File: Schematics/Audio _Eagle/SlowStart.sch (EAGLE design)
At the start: 19 parts

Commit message: slow start updates
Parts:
- added U$4: FUSE, Amplifier_Parts:FUSE
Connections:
- new net N$6: U$2.S2
- net N$1: no longer U$2.S2
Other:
- note added: "fuse will go here"
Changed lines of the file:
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@@
 <part name="GND1" library="supply1" deviceset="GND" device=""/>
 <part name="R2" library="resistor" deviceset="R-US_" device="0207/15" value="100"/>
+<part name="U$4" library="Amplifier_Parts" deviceset="FUSE" device=""/>
 </parts>
 <sheets>
@@
 <text x="81.28" y="71.12" size="1.778" layer="97">Vac+</text>
 <text x="58.42" y="43.18" size="1.778" layer="97">Vac-</text>
+<text x="-10.16" y="73.66" size="1.778" layer="97">fuse will go here</text>
 </plain>
 <instances>
@@
 <instance part="GND1" gate="1" x="81.28" y="50.8" rot="R270"/>
 <instance part="R2" gate="G$1" x="88.9" y="50.8"/>
+<instance part="U$4" gate="G$1" x="5.08" y="66.04"/>
 </instances>
 <busses>
@@
 <net name="N$1" class="0">
 <segment>
-<pinref part="U$2" gate="G$1" pin="S2"/>
-<wire x1="-17.78" y1="71.12" x2="-12.7" y2="71.12" width="0.1524" layer="91"/>
-<wire x1="-12.7" y1="71.12" x2="-12.7" y2="76.2" width="0.1524" layer="91"/>
 <pinref part="U$2" gate="G$1" pin="S3"/>
-<wire x1="-12.7" y1="76.2" x2="-17.78" y2="76.2" width="0.1524" layer="91"/>
+<wire x1="12.7" y1="66.04" x2="12.7" y2="76.2" width="0.1524" layer="91"/>
+<wire x1="12.7" y1="76.2" x2="-17.78" y2="76.2" width="0.1524" layer="91"/>
 </segment>
 </net>
@@
 </segment>
 </net>
+<net name="N$6" class="0">
+<segment>
+<pinref part="U$2" gate="G$1" pin="S2"/>
+<wire x1="-17.78" y1="71.12" x2="-2.54" y2="71.12" width="0.1524" layer="91"/>
+<wire x1="-2.54" y1="71.12" x2="-2.54" y2="66.04" width="0.1524" layer="91"/>
+</segment>
+</net>

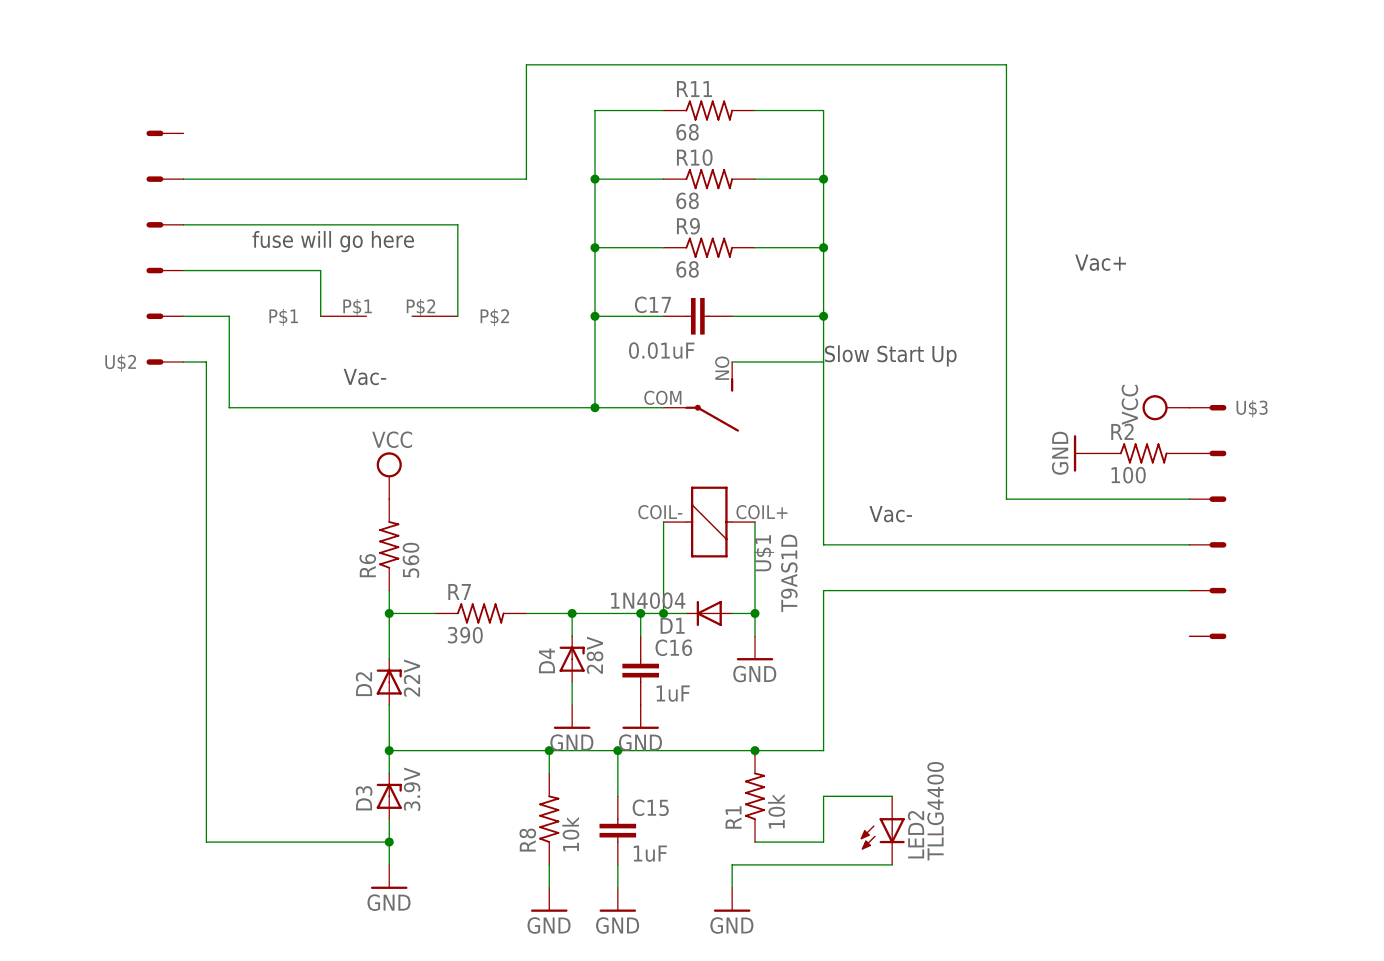
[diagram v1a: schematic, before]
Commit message: updated block diagram
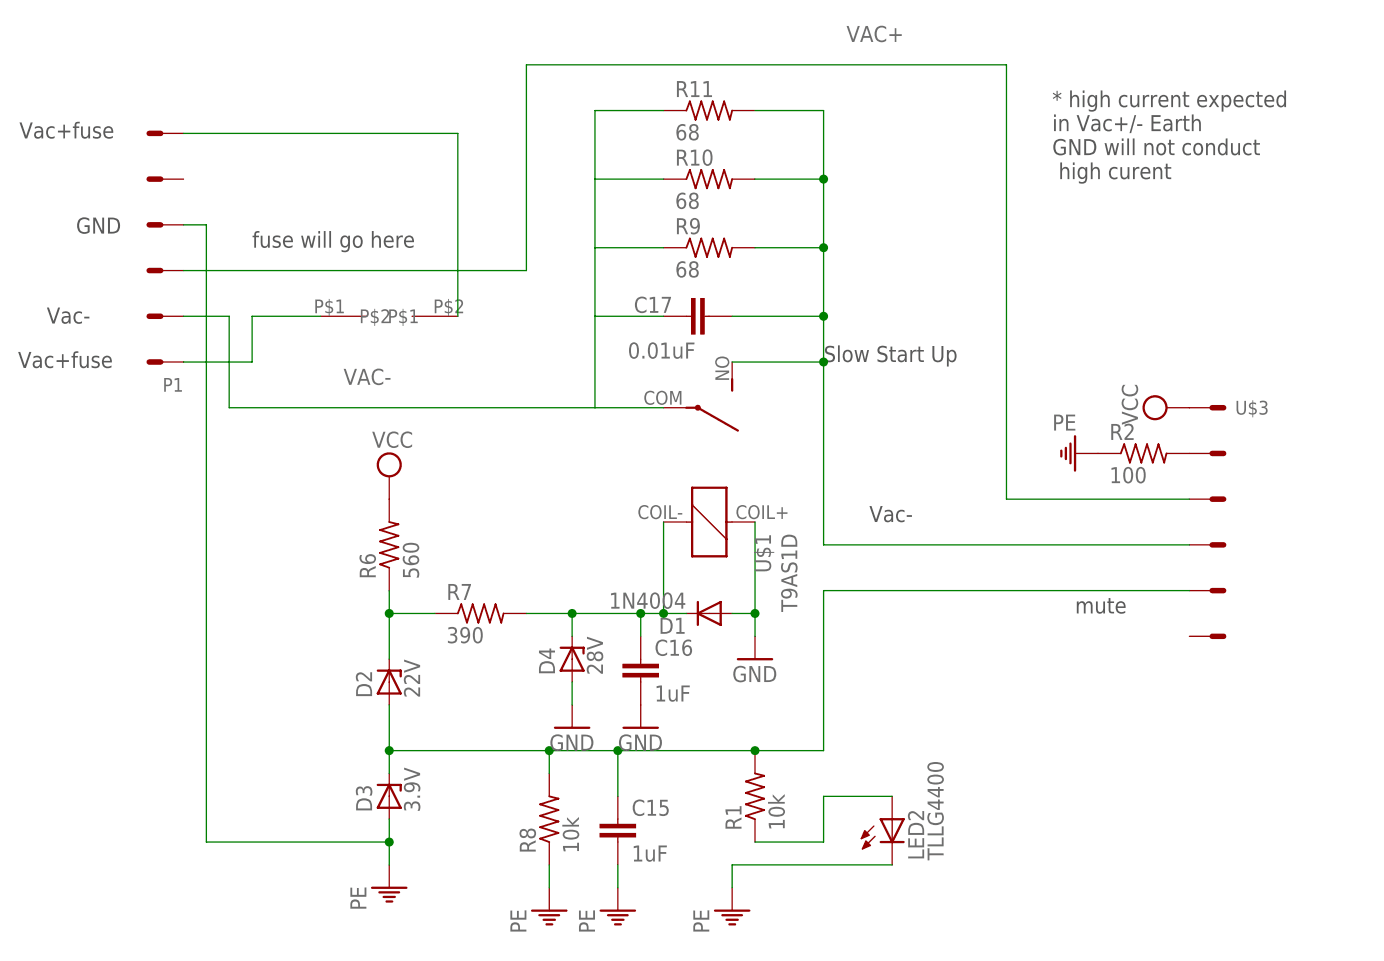
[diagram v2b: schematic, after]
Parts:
- renumbered U$2 to P1
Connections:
- net N$3 renamed VAC-
- removed net N$2: P1.S4, U$3.S2
- new net VAC+: P1.S2, U$3.S2
- net GND: now also P1.S3; no longer P1.S
- net N$1: now also P1.S, U$4.P$1; no longer P1.S3
- net N$6: now also P1.S5, U$4.P$2; no longer P1.S2
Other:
- note added: "* high current expected in Vac+/- Earth GND will not conduct high curent"
- note added: "GND"
- note added: "Vac+fuse"
- note added: "mute"
- note removed: "Vac+"

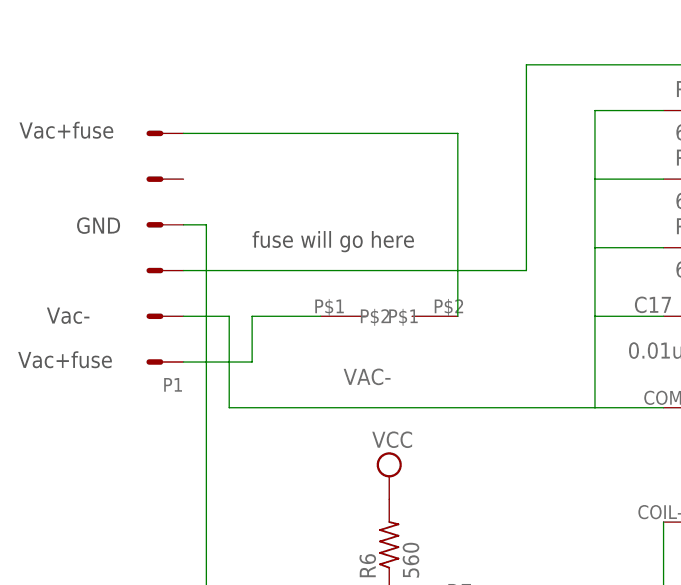
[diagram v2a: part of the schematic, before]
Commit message: created screw terminal and added data sheet
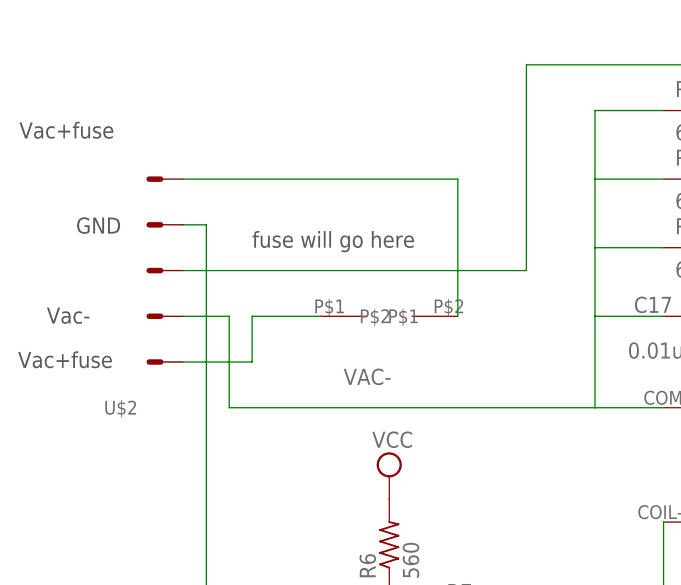
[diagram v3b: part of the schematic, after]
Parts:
- removed P1: MOLEX_6P, Amplifier_Parts:MOLEX_6P
- added U$2: SCREW_TERMINAL_5, Amplifier_Parts:SCREW_TERMINAL_5
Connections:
- removed net N$6: P1.S5, U$4.P$2
- new net N$2: U$2.S5, U$4.P$2
- net GND: now also U$2.S4; no longer P1.S3
- net N$1: now also U$2.S1; no longer P1.S
- net VAC+: now also U$2.S3; no longer P1.S2
- net VAC-: now also U$2.S2; no longer P1.S1
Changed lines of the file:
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@@
 <part name="PE4" library="supply1" deviceset="PE" device=""/>
 <part name="PE5" library="supply1" deviceset="PE" device=""/>
-<part name="P1" library="Amplifier_Parts" deviceset="MOLEX_6P" device=""/>
+<part name="U$2" library="Amplifier_Parts" deviceset="SCREW_TERMINAL_5" device=""/>
 </parts>
 <sheets>
@@
 <instance part="PE4" gate="M" x="43.18" y="0"/>
 <instance part="PE5" gate="M" x="81.28" y="50.8" rot="R270"/>
-<instance part="P1" gate="G$1" x="-25.4" y="66.04" smashed="yes" rot="R180">
-<attribute name="NAME" x="-17.78" y="59.182" size="1.524" layer="95" rot="R180"/>
-</instance>
+<instance part="U$2" gate="G$1" x="-20.32" y="68.58" rot="R180"/>
 </instances>
 <busses>
@@
 <wire x1="-15.24" y1="76.2" x2="-15.24" y2="7.62" width="0.1524" layer="91"/>
 <pinref part="PE1" gate="M" pin="PE"/>
-<pinref part="P1" gate="G$1" pin="S3"/>
+<pinref part="U$2" gate="G$1" pin="S4"/>
 </segment>
 <segment>
@@
 <wire x1="27.94" y1="55.88" x2="35.56" y2="55.88" width="0.1524" layer="91"/>
 <label x="0" y="58.42" size="1.778" layer="95"/>
-<pinref part="P1" gate="G$1" pin="S1"/>
+<pinref part="U$2" gate="G$1" pin="S2"/>
 </segment>
 </net>
@@
 <wire x1="-10.16" y1="66.04" x2="-10.16" y2="60.96" width="0.1524" layer="91"/>
 <wire x1="-10.16" y1="60.96" x2="-17.78" y2="60.96" width="0.1524" layer="91"/>
-<pinref part="P1" gate="G$1" pin="S"/>
-</segment>
-</net>
-<net name="N$6" class="0">
-<segment>
-<pinref part="U$4" gate="G$1" pin="P$2"/>
-<wire x1="12.7" y1="66.04" x2="12.7" y2="86.36" width="0.1524" layer="91"/>
-<wire x1="12.7" y1="86.36" x2="-17.78" y2="86.36" width="0.1524" layer="91"/>
-<pinref part="P1" gate="G$1" pin="S5"/>
+<pinref part="U$2" gate="G$1" pin="S1"/>
 </segment>
 </net>
@@
 <wire x1="73.66" y1="45.72" x2="93.98" y2="45.72" width="0.1524" layer="91"/>
 <label x="55.88" y="96.52" size="1.778" layer="95"/>
-<pinref part="P1" gate="G$1" pin="S2"/>
-</segment>
-</net>
+<pinref part="U$2" gate="G$1" pin="S3"/>
+</segment>
+</net>
+<net name="N$2" class="0">
+<segment>
+<pinref part="U$4" gate="G$1" pin="P$2"/>
+<wire x1="12.7" y1="66.04" x2="12.7" y2="81.28" width="0.1524" layer="91"/>
+<pinref part="U$2" gate="G$1" pin="S5"/>
+<wire x1="12.7" y1="81.28" x2="-17.78" y2="81.28" width="0.1524" layer="91"/>
+</segment>
+</net>
